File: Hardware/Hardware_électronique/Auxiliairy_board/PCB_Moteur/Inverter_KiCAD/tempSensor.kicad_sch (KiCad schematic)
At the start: 3 parts, among them U1201 TCN75A

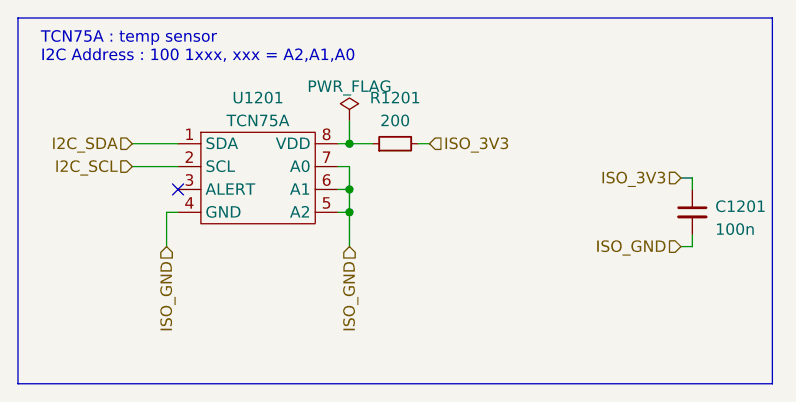
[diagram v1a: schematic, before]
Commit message: update schematic
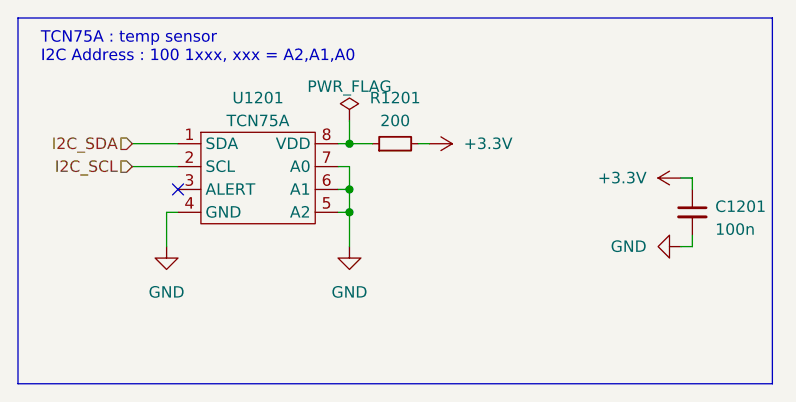
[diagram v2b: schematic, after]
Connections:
- net ISO_3V3 renamed +3.3V
- net ISO_GND renamed GND
